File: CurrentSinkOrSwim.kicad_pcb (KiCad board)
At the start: 2 copper layers, 41.7 x 47.8 mm, 22 parts, among them P1 HEATSINK, P101 CONN_01X02, P102 CONN_01X03, P103 CONN_01X02, Q401 BUK9575, U201 LMV358, U301 LM2931

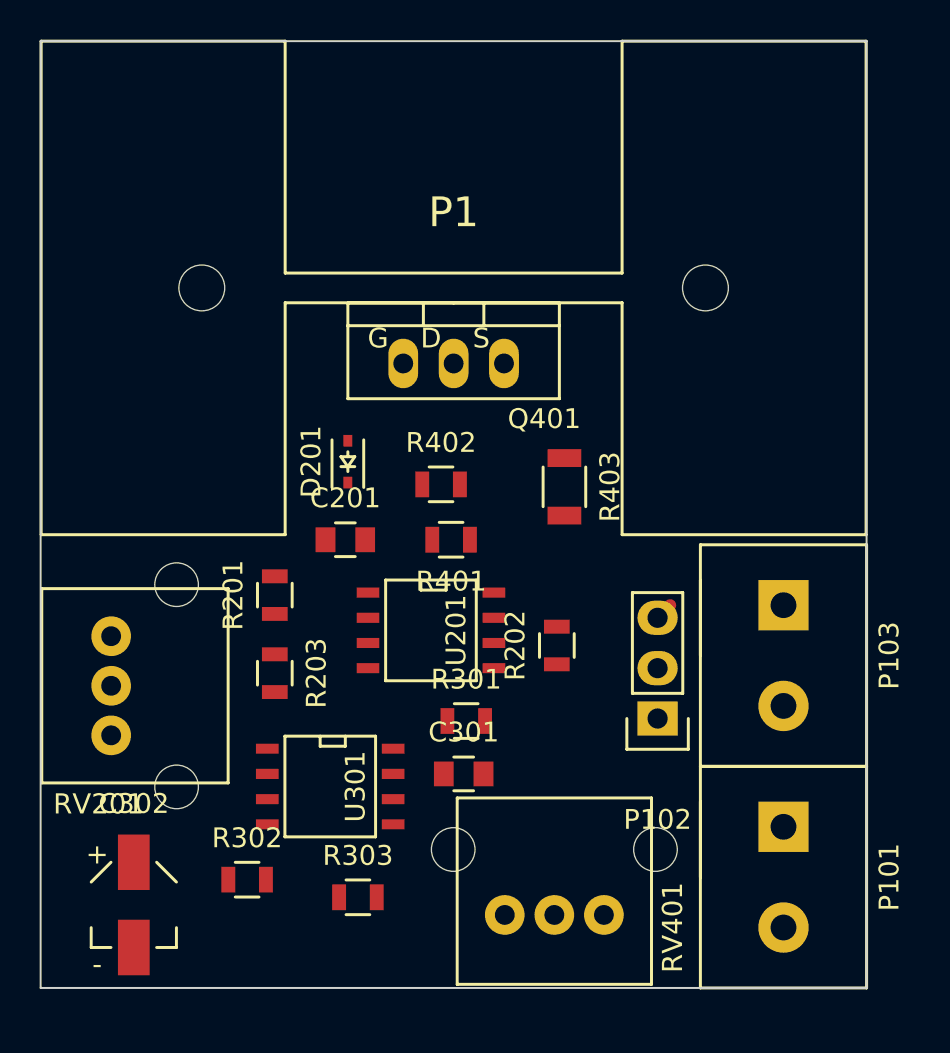
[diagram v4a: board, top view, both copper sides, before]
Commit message: added keepout, ground plane, and moved caps to back side
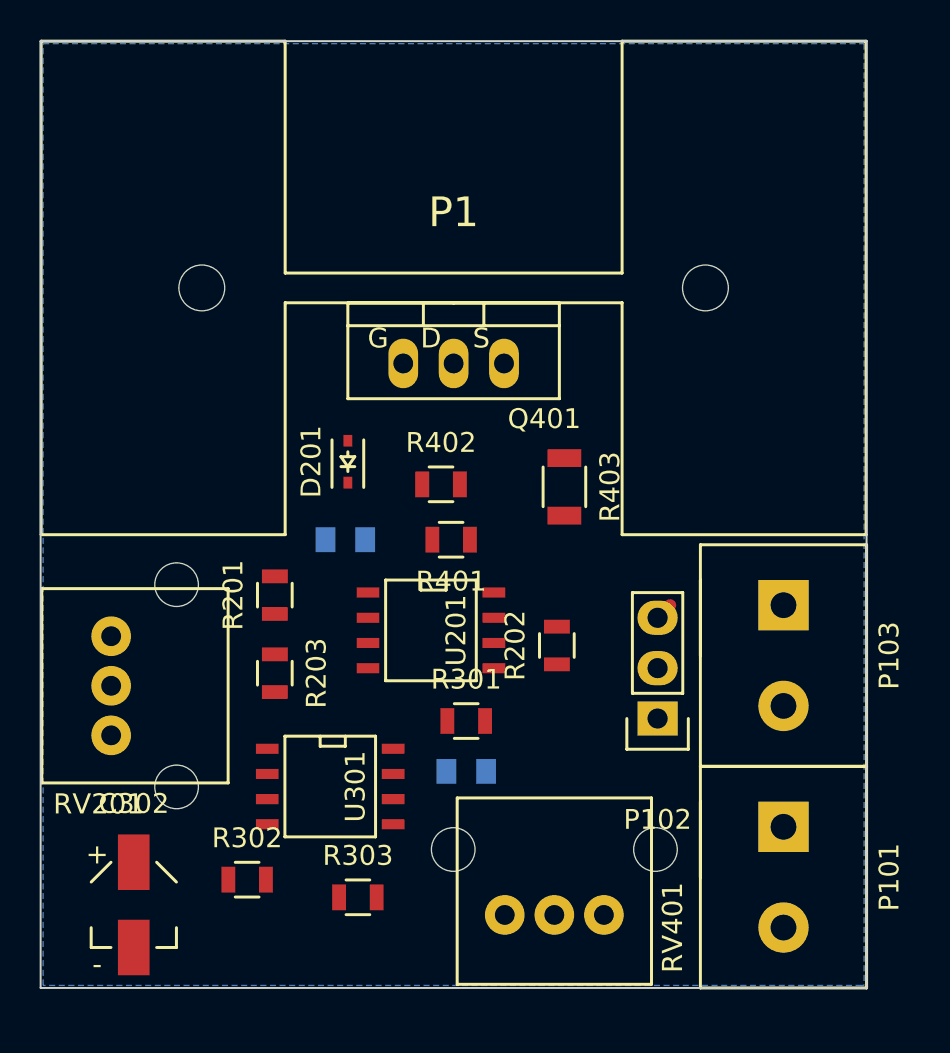
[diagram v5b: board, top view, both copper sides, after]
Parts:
- C201, C301: moved to B.Cu
- moved C301 0.18 mm to (127.6, 72.6)
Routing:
- added copper zone on B.Cu, net GND
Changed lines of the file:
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@@
     (links 42)
     (no_connects 42)
-    (area 100.458199 35.434199 163.074467 120.5278)
+    (area 100.458199 35.434199 150.0508 89.152801)
     (thickness 1.6)
     (drawings 4)
@@
     (44 Edge.Cuts user)
     (45 Margin user)
-    (46 B.CrtYd user)
+    (46 B.CrtYd user hide)
     (47 F.CrtYd user)
-    (48 B.Fab user)
+    (48 B.Fab user hide)
     (49 F.Fab user)
   )
@@
     (trace_clearance 0.254)
     (zone_clearance 0.508)
-    (zone_45_only no)
+    (zone_45_only yes)
     (trace_min 0.254)
     (segment_width 0.2)
@@
     (pad_to_mask_clearance 0)
     (aux_axis_origin 0 0)
-    (visible_elements FFFFD7FF)
+    (visible_elements FFFFDFFF)
     (pcbplotparams
       (layerselection 0x010f0_80000001)
@@
     )
   )
-  (module Capacitors_SMD:C_0805 (layer F.Cu)
+  (module Capacitors_SMD:C_0805 (layer B.Cu)
     (at 121.539 60.96)
     (descr "Capacitor SMD 0805, reflow soldering, AVX (see smccp.pdf)")
     (tags "capacitor 0805")
     (attr smd)
-    (fp_text reference C201 (at 0 -2.1) (layer F.SilkS)
-      (effects (font (size 1 1) (thickness 0.15)))
-    )
-    (fp_text value .1 (at 0 2.1) (layer F.Fab)
-      (effects (font (size 1 1) (thickness 0.15)))
-    )
-    (fp_line (start -1.8 -1) (end 1.8 -1) (layer F.CrtYd) (width 0.05))
-    (fp_line (start -1.8 1) (end 1.8 1) (layer F.CrtYd) (width 0.05))
-    (fp_line (start -1.8 -1) (end -1.8 1) (layer F.CrtYd) (width 0.05))
-    (fp_line (start 1.8 -1) (end 1.8 1) (layer F.CrtYd) (width 0.05))
-    (fp_line (start 0.5 -0.85) (end -0.5 -0.85) (layer F.SilkS) (width 0.15))
-    (fp_line (start -0.5 0.85) (end 0.5 0.85) (layer F.SilkS) (width 0.15))
-    (pad 1 smd rect (at -1 0) (size 1 1.25) (layers F.Cu F.Paste F.Mask)
+    (fp_text reference C201 (at 0 2.1) (layer B.SilkS)
+      (effects (font (size 1 1) (thickness 0.15)) (justify mirror))
+    )
+    (fp_text value .1 (at 0 -2.1) (layer B.Fab)
+      (effects (font (size 1 1) (thickness 0.15)) (justify mirror))
+    )
+    (fp_line (start -1.8 1) (end 1.8 1) (layer B.CrtYd) (width 0.05))
+    (fp_line (start -1.8 -1) (end 1.8 -1) (layer B.CrtYd) (width 0.05))
+    (fp_line (start -1.8 1) (end -1.8 -1) (layer B.CrtYd) (width 0.05))
+    (fp_line (start 1.8 1) (end 1.8 -1) (layer B.CrtYd) (width 0.05))
+    (fp_line (start 0.5 0.85) (end -0.5 0.85) (layer B.SilkS) (width 0.15))
+    (fp_line (start -0.5 -0.85) (end 0.5 -0.85) (layer B.SilkS) (width 0.15))
+    (pad 1 smd rect (at -1 0) (size 1 1.25) (layers B.Cu B.Paste B.Mask)
       (net 1 2.7V))
-    (pad 2 smd rect (at 1 0) (size 1 1.25) (layers F.Cu F.Paste F.Mask)
+    (pad 2 smd rect (at 1 0) (size 1 1.25) (layers B.Cu B.Paste B.Mask)
       (net 2 GND))
     (model Capacitors_SMD.3dshapes/C_0805.wrl
@@
     )
   )
-  (module Capacitors_SMD:C_0805 (layer F.Cu)
-    (at 127.508 72.771)
+  (module Capacitors_SMD:C_0805 (layer B.Cu)
+    (at 127.635 72.644)
     (descr "Capacitor SMD 0805, reflow soldering, AVX (see smccp.pdf)")
     (tags "capacitor 0805")
     (attr smd)
-    (fp_text reference C301 (at 0 -2.1) (layer F.SilkS)
-      (effects (font (size 1 1) (thickness 0.15)))
-    )
-    (fp_text value .1 (at 0 2.1) (layer F.Fab)
-      (effects (font (size 1 1) (thickness 0.15)))
-    )
-    (fp_line (start -1.8 -1) (end 1.8 -1) (layer F.CrtYd) (width 0.05))
-    (fp_line (start -1.8 1) (end 1.8 1) (layer F.CrtYd) (width 0.05))
-    (fp_line (start -1.8 -1) (end -1.8 1) (layer F.CrtYd) (width 0.05))
-    (fp_line (start 1.8 -1) (end 1.8 1) (layer F.CrtYd) (width 0.05))
-    (fp_line (start 0.5 -0.85) (end -0.5 -0.85) (layer F.SilkS) (width 0.15))
-    (fp_line (start -0.5 0.85) (end 0.5 0.85) (layer F.SilkS) (width 0.15))
-    (pad 1 smd rect (at -1 0) (size 1 1.25) (layers F.Cu F.Paste F.Mask)
+    (fp_text reference C301 (at 0 2.1) (layer B.SilkS)
+      (effects (font (size 1 1) (thickness 0.15)) (justify mirror))
+    )
+    (fp_text value .1 (at 0 -2.1) (layer B.Fab)
+      (effects (font (size 1 1) (thickness 0.15)) (justify mirror))
+    )
+    (fp_line (start -1.8 1) (end 1.8 1) (layer B.CrtYd) (width 0.05))
+    (fp_line (start -1.8 -1) (end 1.8 -1) (layer B.CrtYd) (width 0.05))
+    (fp_line (start -1.8 1) (end -1.8 -1) (layer B.CrtYd) (width 0.05))
+    (fp_line (start 1.8 1) (end 1.8 -1) (layer B.CrtYd) (width 0.05))
+    (fp_line (start 0.5 0.85) (end -0.5 0.85) (layer B.SilkS) (width 0.15))
+    (fp_line (start -0.5 -0.85) (end 0.5 -0.85) (layer B.SilkS) (width 0.15))
+    (pad 1 smd rect (at -1 0) (size 1 1.25) (layers B.Cu B.Paste B.Mask)
       (net 3 "/Power Regulation/Vin"))
-    (pad 2 smd rect (at 1 0) (size 1 1.25) (layers F.Cu F.Paste F.Mask)
+    (pad 2 smd rect (at 1 0) (size 1 1.25) (layers B.Cu B.Paste B.Mask)
       (net 2 GND))
     (model Capacitors_SMD.3dshapes/C_0805.wrl
@@
   (segment (start 137.922 64.262) (end 137.287 64.897) (width 0.6096) (layer F.Cu) (net 7))
   (segment (start 143.637 64.262) (end 143.637 63.627) (width 0.254) (layer F.Cu) (net 7))
+  (zone (net 0) (net_name "") (layer F.Cu) (hatch edge 0.508)
+    (connect_pads (clearance 0.508))
+    (min_thickness 0.254)
+    (keepout (tracks not_allowed) (vias not_allowed) (copperpour allowed))
+    (fill (arc_segments 16) (thermal_gap 0.508) (thermal_bridge_width 0.508))
+    (polygon
+      (pts
+        (xy 118.491 47.625) (xy 135.382 47.625) (xy 135.382 35.941) (xy 147.828 35.941) (xy 147.828 60.579)
+        (xy 135.509 60.579) (xy 135.509 49.022) (xy 118.491 49.022) (xy 118.491 60.706) (xy 106.172 60.706)
+        (xy 106.172 35.814) (xy 118.491 35.814) (xy 118.491 47.625)
+      )
+    )
+  )
+  (zone (net 2) (net_name GND) (layer B.Cu) (hatch edge 0.508)
+    (connect_pads (clearance 0.508))
+    (min_thickness 0.254)
+    (fill (arc_segments 16) (thermal_gap 0.508) (thermal_bridge_width 0.508))
+    (polygon
+      (pts
+        (xy 147.574 83.439) (xy 106.299 83.439) (xy 106.299 35.941) (xy 147.701 35.941) (xy 147.701 83.439)
+        (xy 147.574 83.439)
+      )
+    )
+  )
 )

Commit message: possible layout with over half of tracks
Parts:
- moved RV401 18.9 mm to (113.2, 80.8)
- moved R302 15.7 mm to (132.0, 81.5)
- moved R301 14.7 mm to (136.8, 81.7), turned to 180 degrees
- moved U301 13.6 mm to (134.0, 76.7)
- moved R202 13.6 mm to (121.3, 58.2), turned to 270 degrees
- moved C301 12.7 mm to (139.8, 76.2), turned to 270 degrees
- moved C302 12.0 mm to (122.8, 78.7)
- moved R401 11.4 mm to (125.6, 72.3), turned to 90 degrees
- moved C201 10.7 mm to (122.0, 71.6), turned to 180 degrees
- moved R201 6.94 mm to (122.4, 69.1), turned to 180 degrees
- moved R303 5.76 mm to (127.8, 77.6), turned to 90 degrees
- moved R203 4.72 mm to (122.3, 65.8), turned to 180 degrees
- moved U201 4.04 mm to (129.5, 67.2)
- moved D201 3.86 mm to (125.3, 58.2)
- moved R402 1.52 mm to (127.9, 58.2), turned to 270 degrees
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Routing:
- net /Current Control/Current_Sink+: track 1.66 -> 50.3 mm
- net 2.7V: track 0.00 -> 43.1 mm, vias 0 -> 2
- net GND: track 0.00 -> 31.1 mm, vias 0 -> 2
- net Net-(R401-Pad2): track 0.00 -> 27.2 mm
- net Net-(R201-Pad2): track 0.00 -> 19.7 mm
- net Net-(R202-Pad2): track 0.00 -> 10.9 mm
- net /Power Regulation/Vin: track 0.00 -> 10.8 mm
- net Net-(R402-Pad2): track 0.00 -> 10.2 mm
- net /Current Control/FET_Gate: track 0.00 -> 9.69 mm
- net Net-(P101-Pad1): track 0.00 -> 8.88 mm
- net Net-(R302-Pad2): track 0.00 -> 6.86 mm
- net Net-(D201-Pad1): track 0.00 -> 6.48 mm
- net Net-(Q401-PadS): track 0.00 -> 5.38 mm
- net Net-(R301-Pad1): track 0.00 -> 3.28 mm

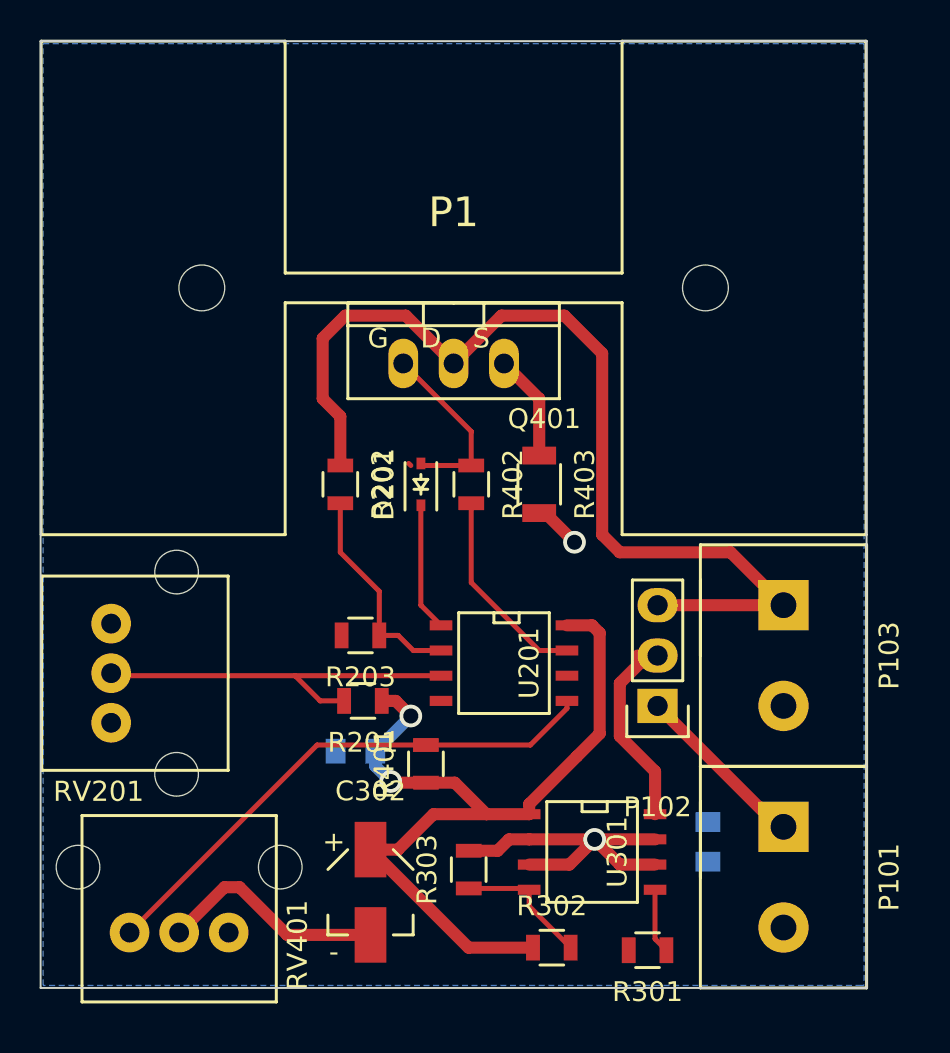
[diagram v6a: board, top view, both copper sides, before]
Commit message: added last ground traces, one backside trace, and vias to ground. passes drc.
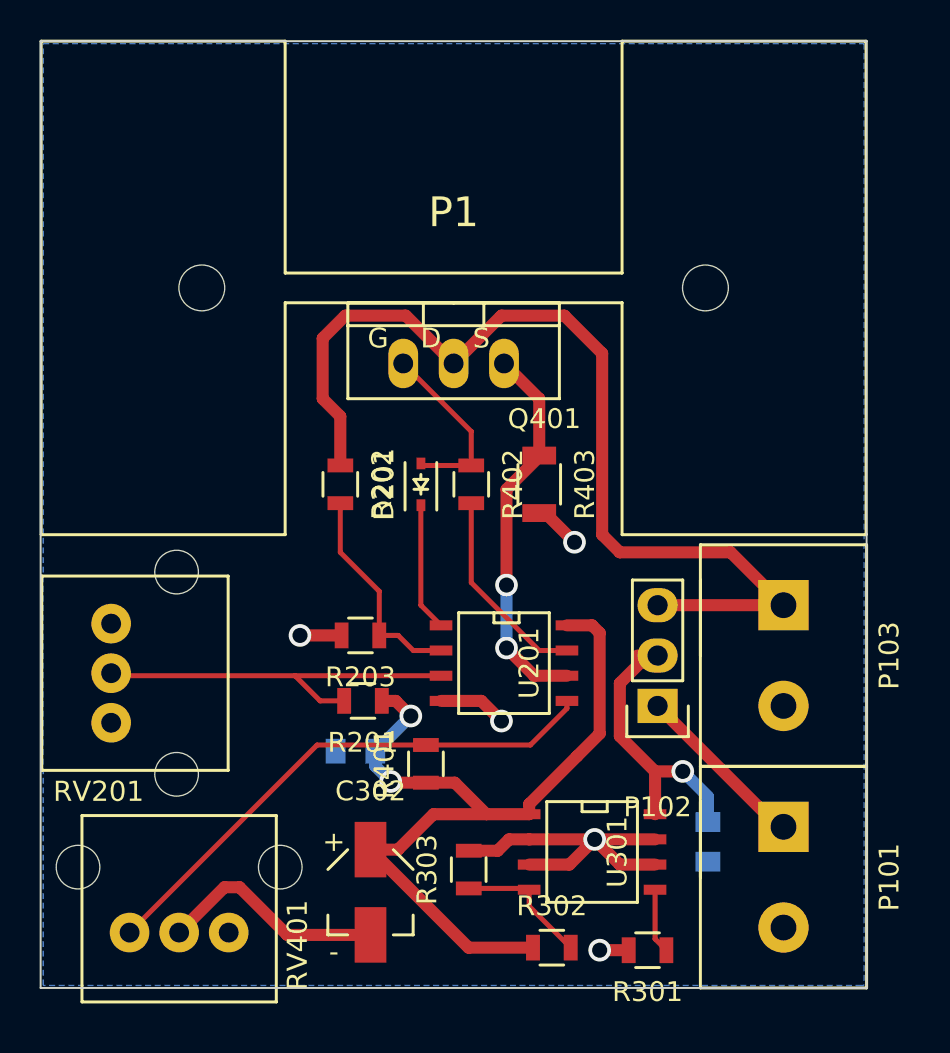
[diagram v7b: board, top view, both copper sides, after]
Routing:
- net Net-(Q401-PadS): track 5.38 -> 19.4 mm, vias 0 -> 2
- net GND: track 31.1 -> 38.2 mm, vias 2 -> 5
- net /Power Regulation/Vin: track 10.8 -> 15.3 mm, vias 0 -> 1
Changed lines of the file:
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@@
   (general
     (links 42)
-    (no_connects 12)
-    (area 100.458199 35.434199 150.0508 89.152801)
+    (no_connects 0)
+    (area 100.458199 35.434199 150.0508 90.041801)
     (thickness 1.6)
     (drawings 4)
-    (tracks 101)
+    (tracks 119)
     (zones 0)
     (modules 22)
@@
     (pad_to_mask_clearance 0)
     (aux_axis_origin 0 0)
-    (visible_elements FFFFDF7F)
+    (visible_elements FFFEDF7F)
     (pcbplotparams
       (layerselection 0x010f0_80000001)
@@
   (gr_line (start 106.172 83.566) (end 147.828 83.566) (angle 90) (layer Edge.Cuts) (width 0.1))
   (gr_line (start 106.172 35.814) (end 106.172 83.566) (angle 90) (layer Edge.Cuts) (width 0.1))
-  (segment (start 124.736 57.111) (end 124.841 57.216) (width 0.254) (layer F.Cu) (net 0))
-  (segment (start 123.047 71.628) (end 123.063 71.628) (width 0.6096) (layer B.Cu) (net 1) (status C00000))
-  (segment (start 123.063 71.628) (end 124.841 69.85) (width 0.6096) (layer B.Cu) (net 1) (status 400000))
-  (segment (start 124.079 69.088) (end 123.378 69.088) (width 0.6096) (layer F.Cu) (net 1) (status 800000))
+  (segment (start 123.047 71.628) (end 123.063 71.628) (width 0.6096) (layer B.Cu) (net 1))
+  (segment (start 123.063 71.628) (end 124.841 69.85) (width 0.6096) (layer B.Cu) (net 1))
+  (segment (start 124.079 69.088) (end 123.378 69.088) (width 0.6096) (layer F.Cu) (net 1))
   (segment (start 124.841 69.85) (end 124.079 69.088) (width 0.6096) (layer F.Cu) (net 1))
   (via (at 124.841 69.85) (size 1.143) (drill 0.762) (layers F.Cu B.Cu) (net 1))
-  (segment (start 125.603 73.213) (end 123.886 73.213) (width 0.6096) (layer F.Cu) (net 1) (status 400000))
-  (segment (start 123.047 72.374) (end 123.047 71.628) (width 0.6096) (layer B.Cu) (net 1) (status 800000))
+  (segment (start 125.603 73.213) (end 123.886 73.213) (width 0.6096) (layer F.Cu) (net 1))
+  (segment (start 123.047 72.374) (end 123.047 71.628) (width 0.6096) (layer B.Cu) (net 1))
   (segment (start 123.825 73.152) (end 123.047 72.374) (width 0.6096) (layer B.Cu) (net 1))
   (via (at 123.825 73.152) (size 1.143) (drill 0.762) (layers F.Cu B.Cu) (net 1))
@@
   (segment (start 131.003 81.534) (end 127.753 81.534) (width 0.6096) (layer F.Cu) (net 1))
   (segment (start 127.753 81.534) (end 122.809 76.59) (width 0.6096) (layer F.Cu) (net 1))
+  (segment (start 135.829 81.661) (end 134.366 81.661) (width 0.6096) (layer F.Cu) (net 2))
+  (via (at 134.366 81.661) (size 1.143) (drill 0.762) (layers F.Cu B.Cu) (net 2))
+  (segment (start 126.365 69.088) (end 128.397 69.088) (width 0.6096) (layer F.Cu) (net 2))
+  (via (at 129.413 70.104) (size 1.143) (drill 0.762) (layers F.Cu B.Cu) (net 2))
+  (segment (start 128.397 69.088) (end 129.413 70.104) (width 0.6096) (layer F.Cu) (net 2))
+  (segment (start 121.351 65.786) (end 119.253 65.786) (width 0.6096) (layer F.Cu) (net 2))
+  (via (at 119.253 65.786) (size 1.143) (drill 0.762) (layers F.Cu B.Cu) (net 2))
   (segment (start 137.16 76.073) (end 134.112 76.073) (width 0.6096) (layer F.Cu) (net 2))
   (segment (start 137.16 77.343) (end 135.382 77.343) (width 0.6096) (layer F.Cu) (net 2))
@@
   (segment (start 131.625 59.616) (end 133.096 61.087) (width 0.6096) (layer F.Cu) (net 2))
   (via (at 133.096 61.087) (size 1.143) (drill 0.762) (layers F.Cu B.Cu) (net 2))
+  (segment (start 137.16 72.644) (end 138.557 72.644) (width 0.6096) (layer F.Cu) (net 3))
+  (segment (start 139.827 73.914) (end 139.827 75.2) (width 0.6096) (layer B.Cu) (net 3))
+  (segment (start 138.557 72.644) (end 139.827 73.914) (width 0.6096) (layer B.Cu) (net 3))
+  (via (at 138.557 72.644) (size 1.143) (drill 0.762) (layers F.Cu B.Cu) (net 3))
   (segment (start 137.287 66.802) (end 136.779 66.802) (width 0.6096) (layer F.Cu) (net 3))
   (segment (start 136.779 66.802) (end 135.382 68.199) (width 0.6096) (layer F.Cu) (net 3))
@@
   (segment (start 135.382 61.595) (end 134.493 60.706) (width 0.6096) (layer F.Cu) (net 7))
   (segment (start 140.97 61.595) (end 135.382 61.595) (width 0.6096) (layer F.Cu) (net 7))
+  (segment (start 131.318 56.716) (end 131.318 56.769) (width 0.6096) (layer F.Cu) (net 8))
+  (segment (start 131.318 56.769) (end 129.667 58.42) (width 0.6096) (layer F.Cu) (net 8))
+  (segment (start 131.064 67.818) (end 132.715 67.818) (width 0.6096) (layer F.Cu) (net 8))
+  (segment (start 129.667 66.421) (end 131.064 67.818) (width 0.6096) (layer F.Cu) (net 8))
+  (via (at 129.667 66.421) (size 1.143) (drill 0.762) (layers F.Cu B.Cu) (net 8))
+  (segment (start 129.667 63.246) (end 129.667 66.421) (width 0.6096) (layer B.Cu) (net 8))
+  (via (at 129.667 63.246) (size 1.143) (drill 0.762) (layers F.Cu B.Cu) (net 8))
+  (segment (start 129.667 58.42) (end 129.667 63.246) (width 0.6096) (layer F.Cu) (net 8))
   (segment (start 129.54 52.07) (end 131.318 53.848) (width 0.6096) (layer F.Cu) (net 8))
   (segment (start 131.318 53.848) (end 131.318 56.716) (width 0.6096) (layer F.Cu) (net 8))
@@
     (connect_pads (clearance 0.508))
     (min_thickness 0.254)
-    (fill (arc_segments 16) (thermal_gap 0.508) (thermal_bridge_width 0.508))
+    (fill yes (arc_segments 16) (thermal_gap 0.508) (thermal_bridge_width 0.508))
     (polygon
       (pts
